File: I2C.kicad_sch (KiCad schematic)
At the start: 12 parts, among them U9 TCA9548AMRGER

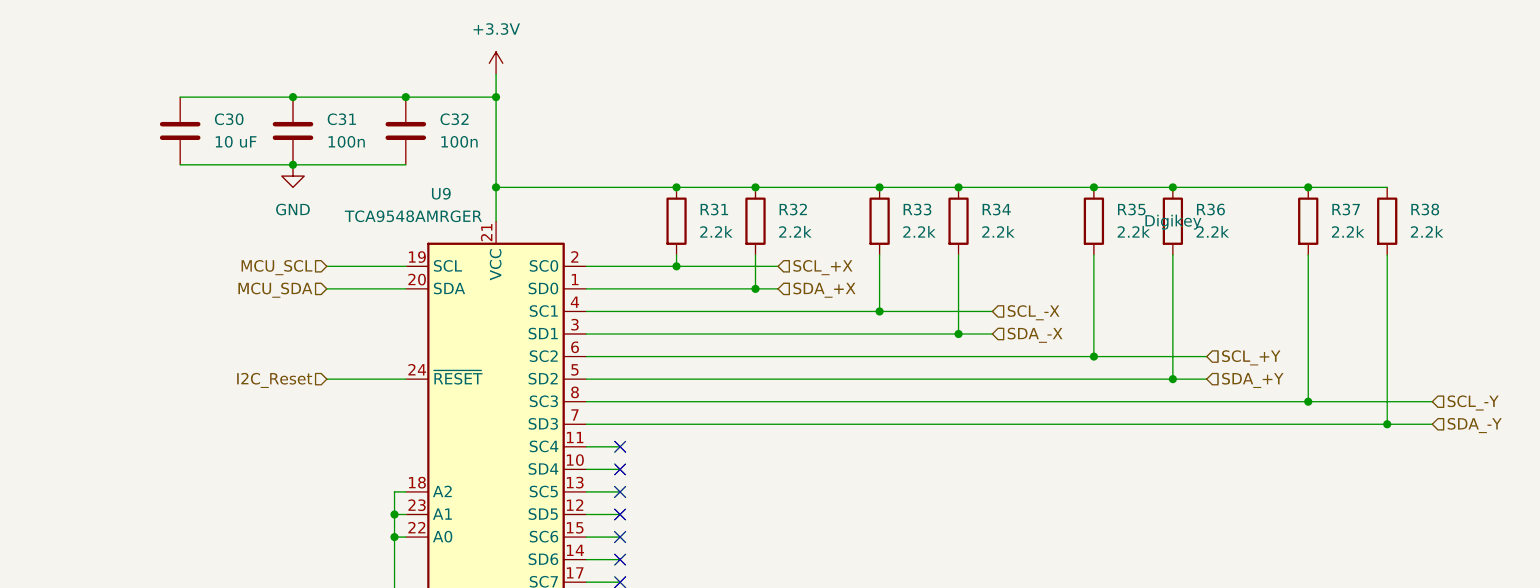
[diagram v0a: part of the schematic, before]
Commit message: Efuses for this board and Battery board
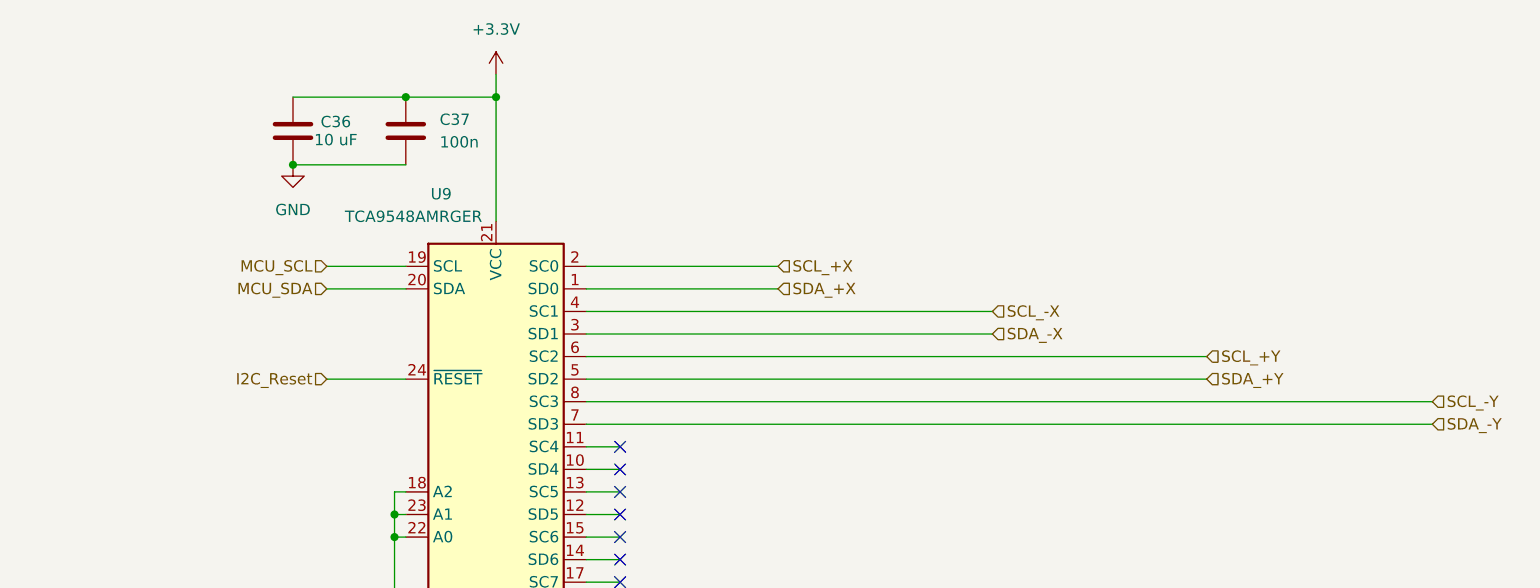
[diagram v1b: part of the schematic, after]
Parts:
- removed C30: 10 uF, zLibrary:CAP_C1210C_X7R_2S_FW_KEM-M, symbol Device:C
- removed C31: 100n, Capacitor_SMD:C_0603_1608Metric, symbol Device:C
- removed R31, R32, R33, R34, R35, R36, R37, R38: 2.2k, Resistor_SMD:R_0603_1608Metric, symbol Device:R
- added C36: 10 uF, Capacitor_SMD:C_0603_1608Metric, symbol Device:C
- renumbered C32 to C37
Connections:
- net +3.3V: now also C36.2
- net GND: now also C36.1

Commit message: Mostly done routing, still yet to start DRC
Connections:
- net SCL_-X: now also U9.17 (SC7); no longer U9.4 (SC1)
- net SDA_-X: now also U9.16 (SD7); no longer U9.3 (SD1)
- no-connect marks 8 -> 6
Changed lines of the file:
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@@
-	)
-	(no_connect
-		(at 143.51 109.22)
 	)
 	(no_connect
@@
 		(at 143.51 99.06)
 	)
-	(no_connect
-		(at 143.51 106.68)
-	)
 	(wire
 		(pts
@@
 	(wire
 		(pts
-			(xy 139.7 76.2) (xy 185.42 76.2)
-		)
-		(stroke
-			(width 0)
-			(type default)
-		)
-	)
-	(wire
-		(pts
 			(xy 139.7 91.44) (xy 143.51 91.44)
 		)
@@
 	(wire
 		(pts
-			(xy 139.7 78.74) (xy 185.42 78.74)
-		)
-		(stroke
-			(width 0)
-			(type default)
-		)
-	)
-	(wire
-		(pts
 			(xy 118.11 99.06) (xy 118.11 101.6)
 		)
@@
 		)
 	)
+	(hierarchical_label "SDA_-X"
+		(shape input)
+		(at 143.51 109.22 0)
+		(effects
+			(font
+				(size 1.27 1.27)
+			)
+			(justify left)
+		)
+	)
 	(hierarchical_label "I2C_Reset"
 		(shape input)
@@
 		)
 	)
+	(hierarchical_label "SDA_+X"
+		(shape input)
+		(at 161.29 73.66 0)
+		(effects
+			(font
+				(size 1.27 1.27)
+			)
+			(justify left)
+		)
+	)
 	(hierarchical_label "SCL_-X"
 		(shape input)
-		(at 185.42 76.2 0)
-		(effects
-			(font
-				(size 1.27 1.27)
-			)
-			(justify left)
-		)
-	)
-	(hierarchical_label "SDA_+X"
-		(shape input)
-		(at 161.29 73.66 0)
-		(effects
-			(font
-				(size 1.27 1.27)
-			)
-			(justify left)
-		)
-	)
-	(hierarchical_label "SDA_-X"
-		(shape input)
-		(at 185.42 78.74 0)
-		(effects
-			(font
+		(at 143.51 106.68 0)
+		(effects
+			(font

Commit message: README and reorganized
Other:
- note added: "I2C MUX"
- moved on the sheet: C36, C37, U9
